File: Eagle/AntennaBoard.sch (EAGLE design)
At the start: 8 parts, among them IC1 MEGA8-P, IC2 MAX487*

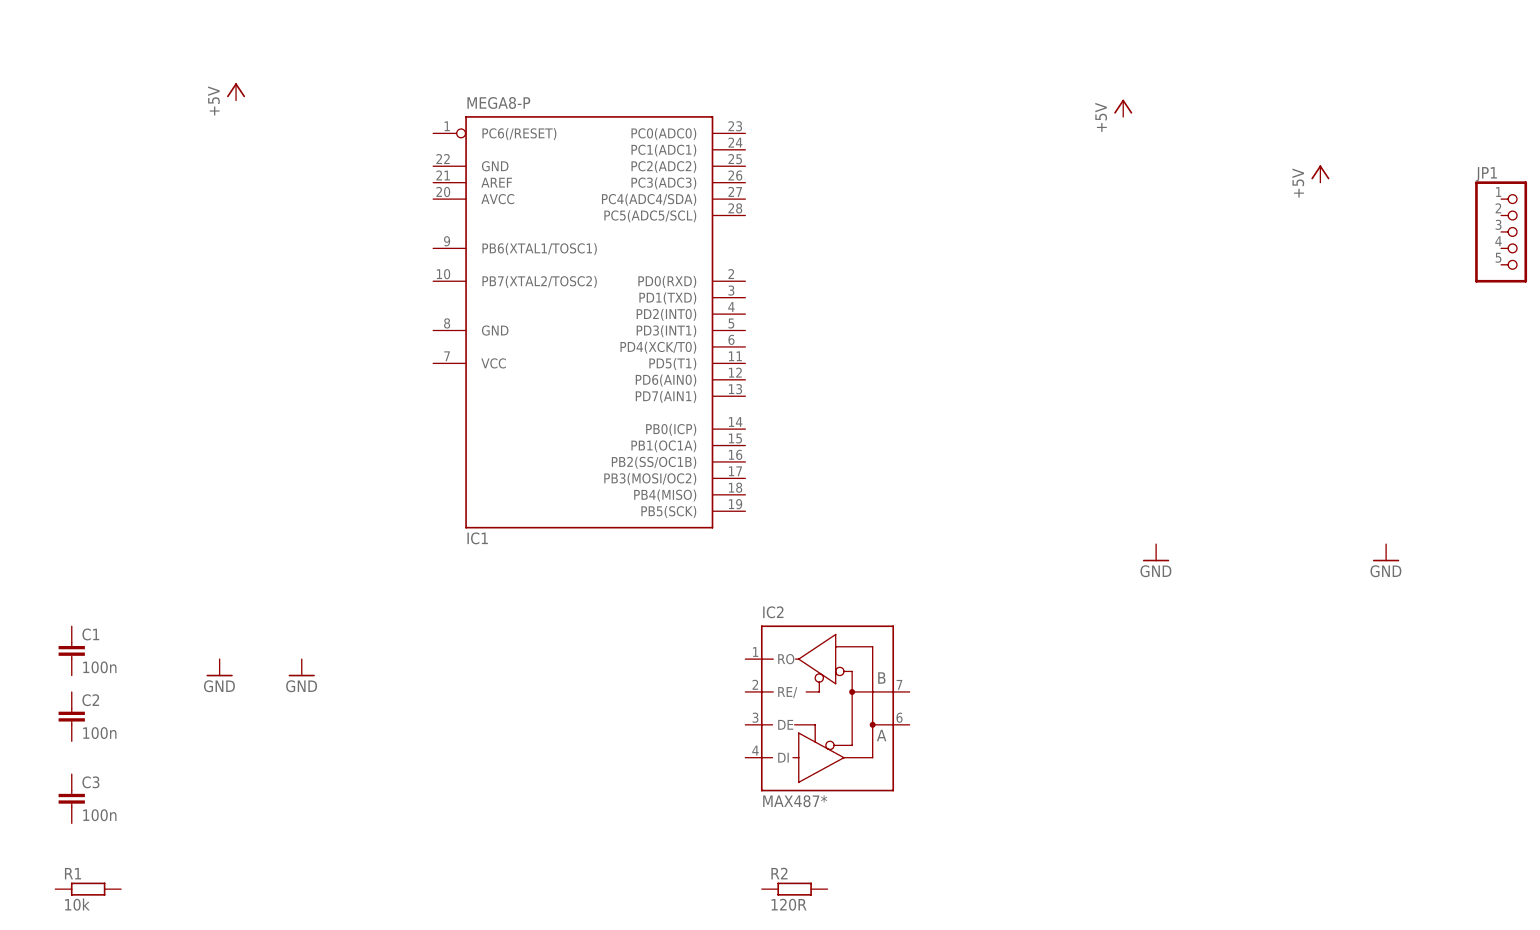
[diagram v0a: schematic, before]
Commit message: - AntennaBoard: finalized (?) and first board layout
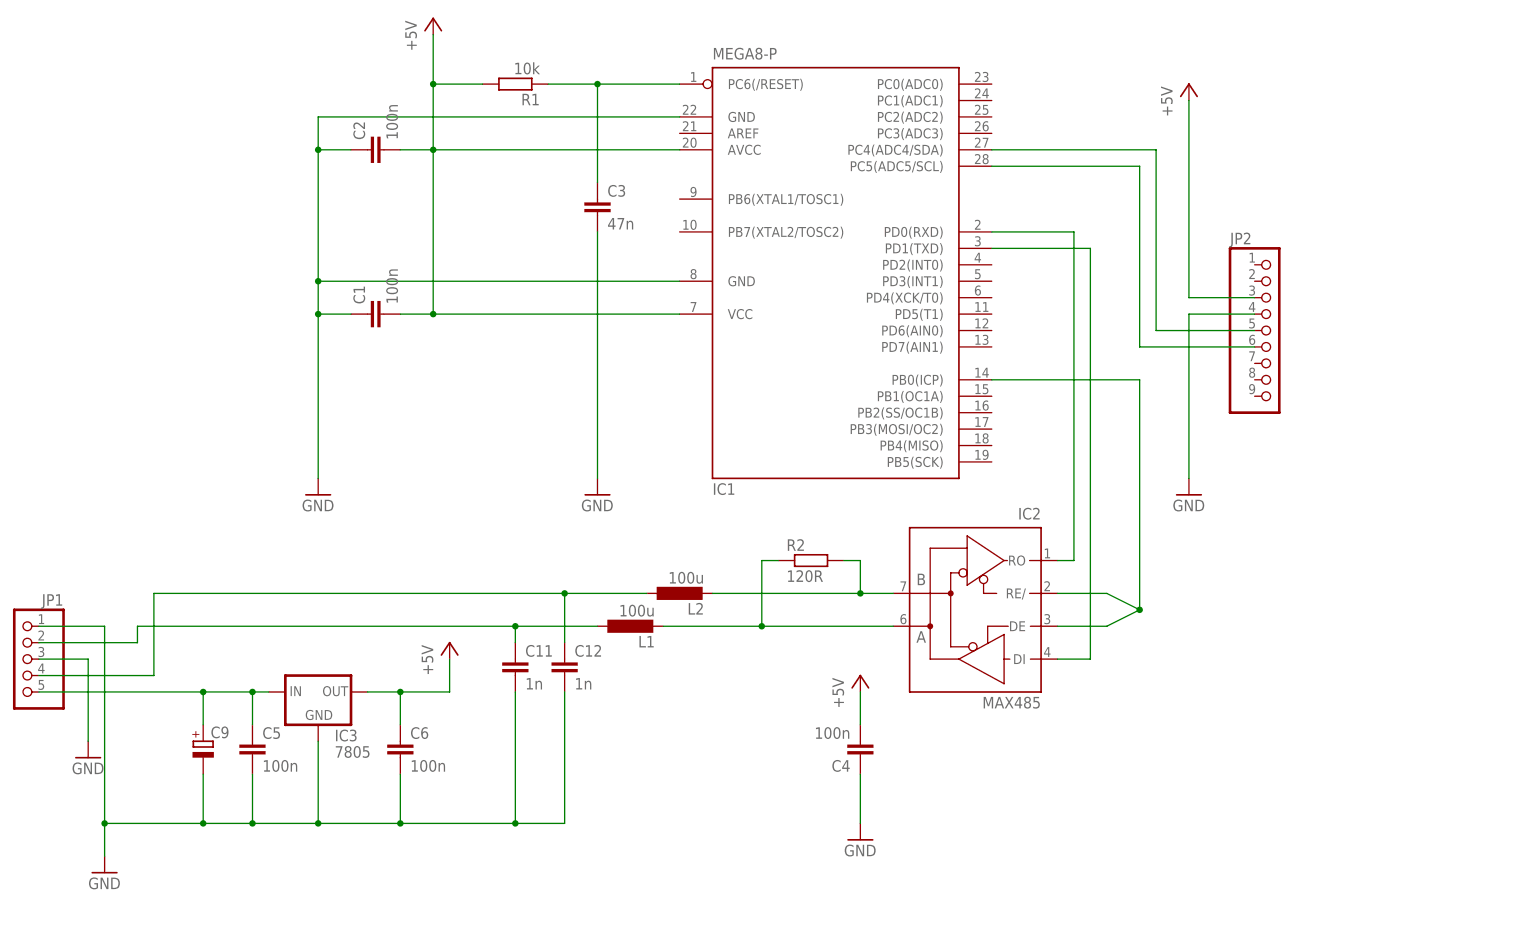
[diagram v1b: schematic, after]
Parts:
- added C11, C12: 1n, rcl:C-EU025-024X044
- added C4, C5, C6: 100n, rcl:C-EU050-024X044
- added C9: (no value), rcl:CPOL-EUE5-10.5
- added IC3: 7805, v-reg:78XXL
- added JP2: (no value), pinhead:PINHD-1X9
- added L1, L2: 100u, rcl:L-EU0207/12
- C3: value 100n -> 47n
- IC2: value MAX487* -> MAX485
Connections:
- new net +5V: C1.2, C2.2, C4.2, C6.1, IC1.AVCC, IC1.VCC@1, IC3.OUT, JP2.3, R1.2
- new net GND: C1.1, C11.2, C12.2, C2.1, C3.2, C4.1, C5.2, C6.2, C9.-, IC1.GND, IC1.GND@1, IC3.GND, JP1.1, JP1.3, JP2.4
- new net N$1: C5.1, C9.+, IC3.IN, JP1.5
- new net N$10: IC2G$1.B, L2.2, R2.2
- new net N$11: C11.1, JP1.2, L1.1
- new net N$2: IC2G$1.A, L1.2, R2.1
- new net N$3: C12.1, JP1.4, L2.1
- new net N$4: IC1.PC5(ADC5/SCL), JP2.6
- new net N$5: C3.1, IC1.PC6(/RESET), R1.1
- new net N$6: IC1.PC4(ADC4/SDA), JP2.5
- new net N$7: IC1.PB0(ICP), IC2G$1.DE, IC2G$1.RE/
- new net N$8: IC1.PD0(RXD), IC2G$1.RO
- new net N$9: IC1.PD1(TXD), IC2G$1.DI
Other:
- moved on the sheet: C1, C2, C3, IC1, IC2, JP1, R1, R2

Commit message: - IPS-Header added to AntennaBoard, U.Radig layout
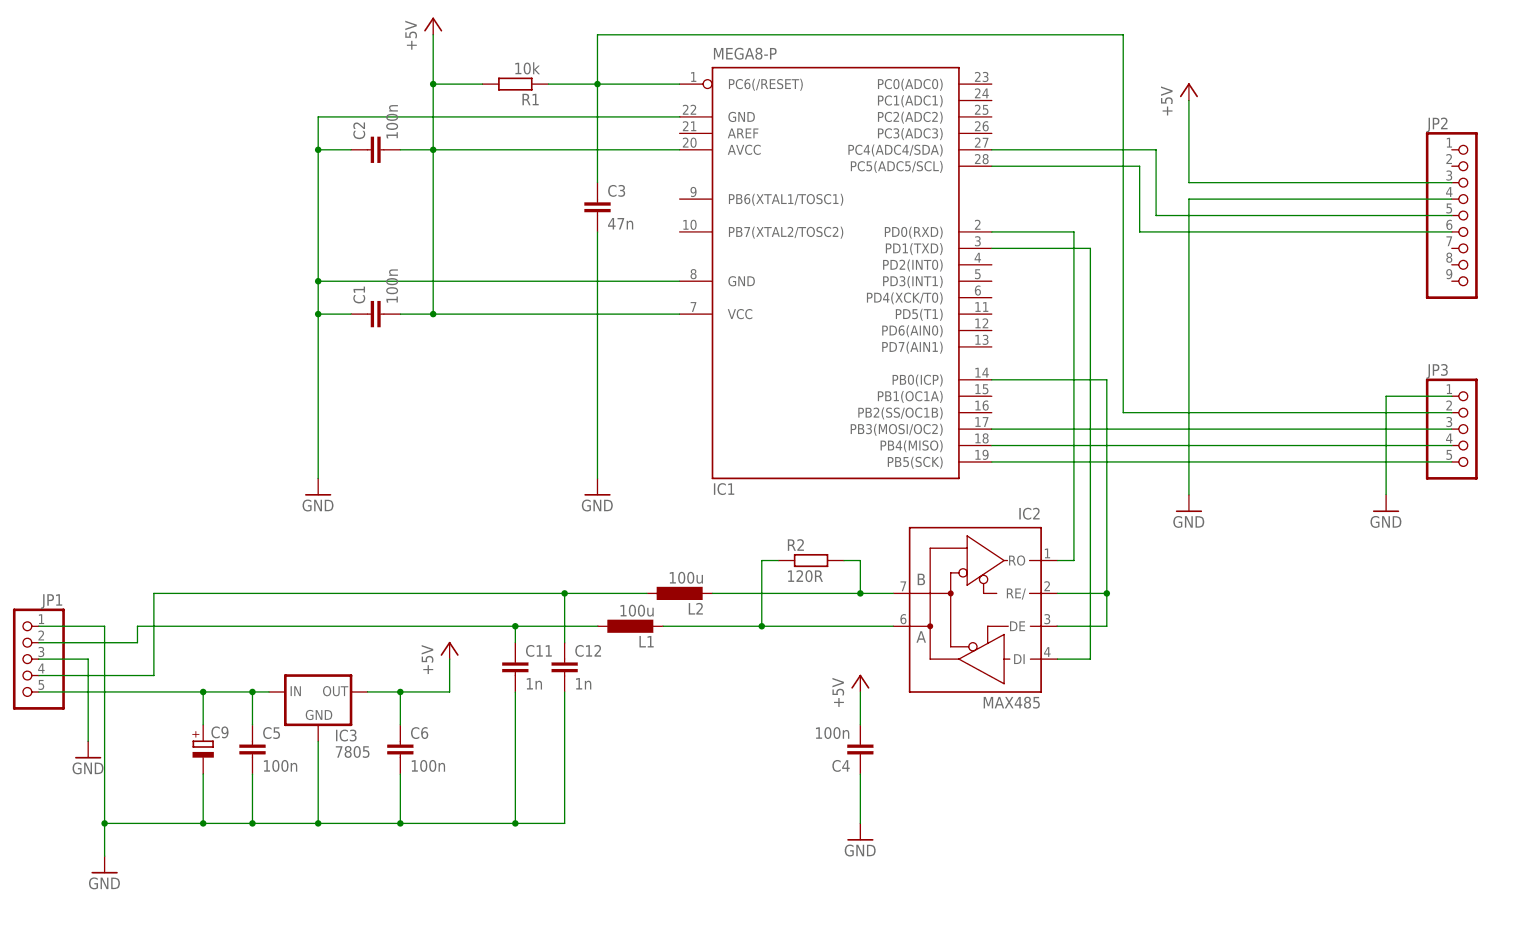
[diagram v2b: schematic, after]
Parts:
- added JP3: (no value), pinhead:PINHD-1X5
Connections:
- new net N$13: IC1.PB3(MOSI/OC2), JP3.3
- new net N$14: IC1.PB4(MISO), JP3.4
- new net N$15: IC1.PB5(SCK), JP3.5
- net GND: now also JP3.1
- net N$5: now also JP3.2
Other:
- moved on the sheet: JP2
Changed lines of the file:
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@@
 <part name="L2" library="rcl" deviceset="L-EU" device="0207/12" value="100u"/>
 <part name="GND3" library="supply1" deviceset="GND" device=""/>
+<part name="JP3" library="pinhead" deviceset="PINHD-1X5" device=""/>
+<part name="GND7" library="supply1" deviceset="GND" device=""/>
 </parts>
 <sheets>
@@
 <instance part="GND1" gate="1" x="58.42" y="104.14"/>
 <instance part="GND2" gate="1" x="25.4" y="45.72"/>
-<instance part="GND4" gate="1" x="193.04" y="104.14"/>
+<instance part="GND4" gate="1" x="193.04" y="101.6"/>
 <instance part="C4" gate="G$1" x="142.24" y="63.5" rot="R180"/>
-<instance part="JP2" gate="A" x="205.74" y="129.54"/>
+<instance part="JP2" gate="A" x="236.22" y="147.32"/>
 <instance part="IC3" gate="A" x="58.42" y="73.66"/>
 <instance part="C5" gate="G$1" x="48.26" y="66.04"/>
@@
 <instance part="L2" gate="G$1" x="114.3" y="88.9" rot="R90"/>
 <instance part="GND3" gate="1" x="101.6" y="104.14"/>
+<instance part="JP3" gate="A" x="236.22" y="114.3"/>
+<instance part="GND7" gate="1" x="223.52" y="101.6"/>
 </instances>
 <busses>
@@
 <segment>
 <pinref part="JP2" gate="A" pin="4"/>
-<wire x1="203.2" y1="132.08" x2="193.04" y2="132.08" width="0.1524" layer="91"/>
+<wire x1="233.68" y1="149.86" x2="193.04" y2="149.86" width="0.1524" layer="91"/>
 <pinref part="GND4" gate="1" pin="GND"/>
-<wire x1="193.04" y1="132.08" x2="193.04" y2="106.68" width="0.1524" layer="91"/>
+<wire x1="193.04" y1="149.86" x2="193.04" y2="104.14" width="0.1524" layer="91"/>
 </segment>
 <segment>
@@
 <pinref part="C3" gate="G$1" pin="2"/>
 <wire x1="101.6" y1="106.68" x2="101.6" y2="144.78" width="0.1524" layer="91"/>
+</segment>
+<segment>
+<pinref part="JP3" gate="A" pin="1"/>
+<wire x1="233.68" y1="119.38" x2="223.52" y2="119.38" width="0.1524" layer="91"/>
+<pinref part="GND7" gate="1" pin="GND"/>
+<wire x1="223.52" y1="119.38" x2="223.52" y2="104.14" width="0.1524" layer="91"/>
 </segment>
 </net>
@@
 <wire x1="101.6" y1="167.64" x2="101.6" y2="152.4" width="0.1524" layer="91"/>
 <junction x="101.6" y="167.64"/>
+<pinref part="JP3" gate="A" pin="2"/>
+<wire x1="233.68" y1="116.84" x2="182.88" y2="116.84" width="0.1524" layer="91"/>
+<wire x1="182.88" y1="116.84" x2="182.88" y2="175.26" width="0.1524" layer="91"/>
+<wire x1="182.88" y1="175.26" x2="101.6" y2="175.26" width="0.1524" layer="91"/>
+<wire x1="101.6" y1="175.26" x2="101.6" y2="167.64" width="0.1524" layer="91"/>
 </segment>
 </net>
@@
 <segment>
 <pinref part="JP2" gate="A" pin="3"/>
-<wire x1="203.2" y1="134.62" x2="193.04" y2="134.62" width="0.1524" layer="91"/>
+<wire x1="233.68" y1="152.4" x2="193.04" y2="152.4" width="0.1524" layer="91"/>
 <pinref part="P+3" gate="1" pin="+5V"/>
-<wire x1="193.04" y1="134.62" x2="193.04" y2="165.1" width="0.1524" layer="91"/>
+<wire x1="193.04" y1="152.4" x2="193.04" y2="165.1" width="0.1524" layer="91"/>
 </segment>
 </net>
@@
 <pinref part="IC1" gate="G$1" pin="PC5(ADC5/SCL)"/>
 <wire x1="162.56" y1="154.94" x2="185.42" y2="154.94" width="0.1524" layer="91"/>
-<wire x1="185.42" y1="154.94" x2="185.42" y2="127" width="0.1524" layer="91"/>
+<wire x1="185.42" y1="154.94" x2="185.42" y2="144.78" width="0.1524" layer="91"/>
 <pinref part="JP2" gate="A" pin="6"/>
-<wire x1="185.42" y1="127" x2="203.2" y2="127" width="0.1524" layer="91"/>
+<wire x1="185.42" y1="144.78" x2="233.68" y2="144.78" width="0.1524" layer="91"/>
 </segment>
 </net>
@@
 <pinref part="IC1" gate="G$1" pin="PC4(ADC4/SDA)"/>
 <wire x1="162.56" y1="157.48" x2="187.96" y2="157.48" width="0.1524" layer="91"/>
-<wire x1="187.96" y1="157.48" x2="187.96" y2="129.54" width="0.1524" layer="91"/>
+<wire x1="187.96" y1="157.48" x2="187.96" y2="147.32" width="0.1524" layer="91"/>
 <pinref part="JP2" gate="A" pin="5"/>
-<wire x1="187.96" y1="129.54" x2="203.2" y2="129.54" width="0.1524" layer="91"/>
+<wire x1="187.96" y1="147.32" x2="233.68" y2="147.32" width="0.1524" layer="91"/>
 </segment>
 </net>
 <net name="N$7" class="0">
 <segment>
+<wire x1="180.34" y1="88.9" x2="180.34" y2="121.92" width="0.1524" layer="91"/>
+<pinref part="IC1" gate="G$1" pin="PB0(ICP)"/>
+<wire x1="180.34" y1="121.92" x2="162.56" y2="121.92" width="0.1524" layer="91"/>
 <pinref part="IC2" gate="G$1" pin="RE/"/>
 <wire x1="172.72" y1="88.9" x2="180.34" y2="88.9" width="0.1524" layer="91"/>
-<wire x1="180.34" y1="88.9" x2="185.42" y2="86.36" width="0.1524" layer="91"/>
 <pinref part="IC2" gate="G$1" pin="DE"/>
-<wire x1="185.42" y1="86.36" x2="180.34" y2="83.82" width="0.1524" layer="91"/>
 <wire x1="180.34" y1="83.82" x2="172.72" y2="83.82" width="0.1524" layer="91"/>
-<junction x="185.42" y="86.36"/>
-<wire x1="185.42" y1="86.36" x2="185.42" y2="121.92" width="0.1524" layer="91"/>
-<pinref part="IC1" gate="G$1" pin="PB0(ICP)"/>
-<wire x1="185.42" y1="121.92" x2="162.56" y2="121.92" width="0.1524" layer="91"/>
+<wire x1="180.34" y1="88.9" x2="180.34" y2="83.82" width="0.1524" layer="91"/>
+<junction x="180.34" y="88.9"/>
 </segment>
 </net>
@@
 </segment>
 </net>
+<net name="N$13" class="0">
+<segment>
+<pinref part="IC1" gate="G$1" pin="PB3(MOSI/OC2)"/>
+<pinref part="JP3" gate="A" pin="3"/>
+<wire x1="162.56" y1="114.3" x2="233.68" y2="114.3" width="0.1524" layer="91"/>
+</segment>
+</net>
+<net name="N$14" class="0">
+<segment>
+<pinref part="JP3" gate="A" pin="4"/>
+<pinref part="IC1" gate="G$1" pin="PB4(MISO)"/>
+<wire x1="233.68" y1="111.76" x2="162.56" y2="111.76" width="0.1524" layer="91"/>
+</segment>
+</net>
+<net name="N$15" class="0">
+<segment>
+<pinref part="IC1" gate="G$1" pin="PB5(SCK)"/>
+<pinref part="JP3" gate="A" pin="5"/>
+<wire x1="162.56" y1="109.22" x2="233.68" y2="109.22" width="0.1524" layer="91"/>
+</segment>
+</net>

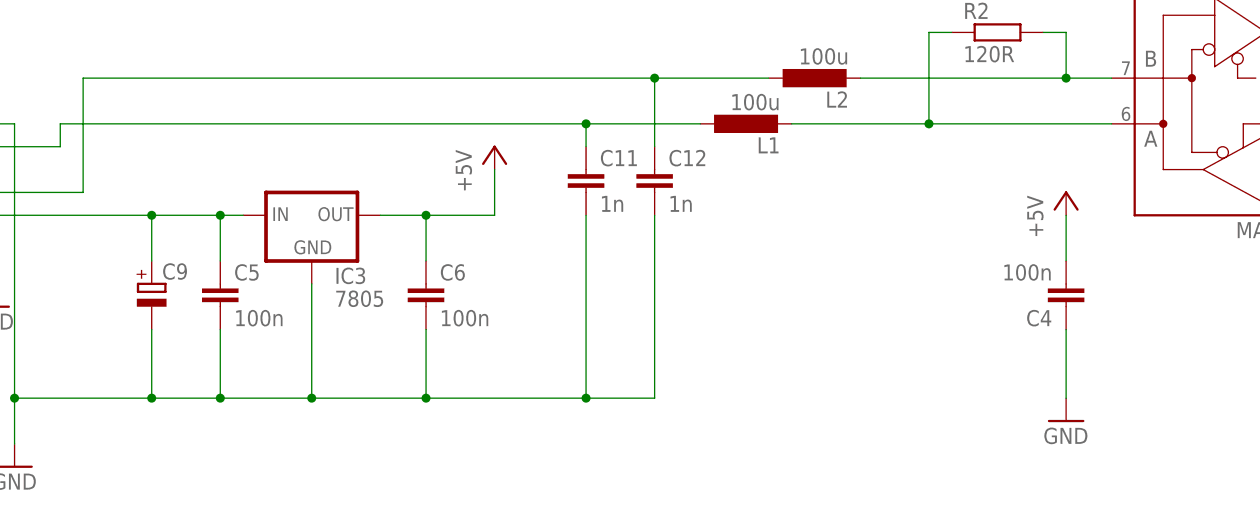
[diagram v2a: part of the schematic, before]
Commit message: - AntennaBoard: ERC errors fixed, worked on board and DRC - PowerSupply: ERC & DRC errors fixed
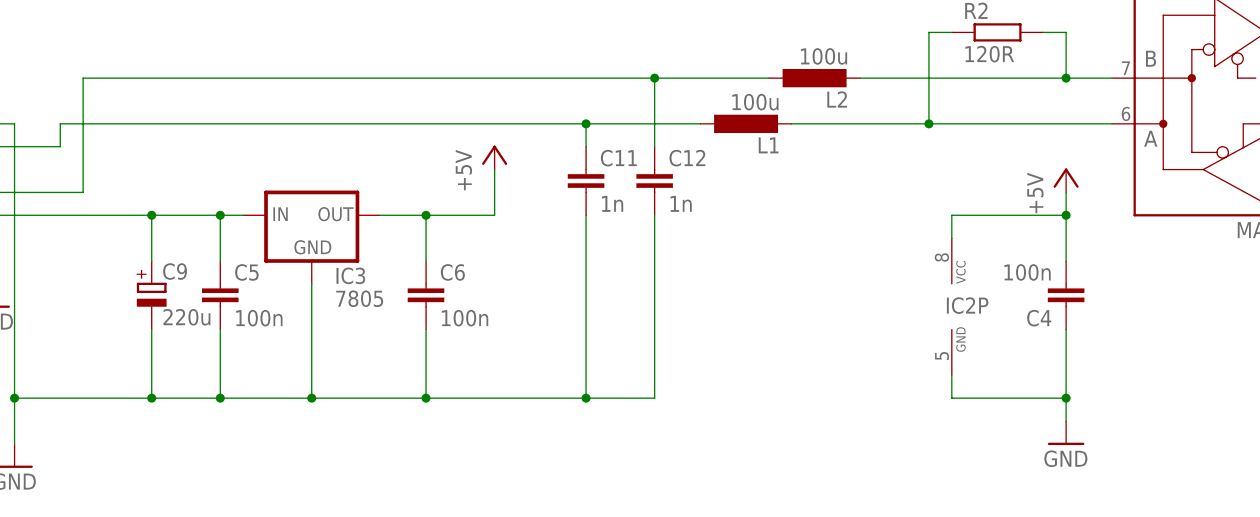
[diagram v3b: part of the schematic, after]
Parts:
- C9: value (none) -> 220u
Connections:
- net +5V: now also IC2P.VCC
- net GND: now also IC2P.GND
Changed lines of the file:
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@@
 <layer number="91" name="Nets" color="2" fill="1" visible="yes" active="yes"/>
 <layer number="92" name="Busses" color="1" fill="1" visible="yes" active="yes"/>
-<layer number="93" name="Pins" color="2" fill="1" visible="no" active="yes"/>
+<layer number="93" name="Pins" color="2" fill="1" visible="yes" active="yes"/>
 <layer number="94" name="Symbols" color="4" fill="1" visible="yes" active="yes"/>
 <layer number="95" name="Names" color="7" fill="1" visible="yes" active="yes"/>
@@
 <part name="C5" library="rcl" deviceset="C-EU" device="050-024X044" value="100n"/>
 <part name="C6" library="rcl" deviceset="C-EU" device="050-024X044" value="100n"/>
-<part name="C9" library="rcl" deviceset="CPOL-EU" device="E5-10.5"/>
+<part name="C9" library="rcl" deviceset="CPOL-EU" device="E5-10.5" value="220u"/>
 <part name="P+4" library="supply1" deviceset="+5V" device=""/>
 <part name="GND5" library="supply1" deviceset="GND" device=""/>
@@
 <instance part="P+4" gate="1" x="78.74" y="81.28"/>
 <instance part="GND5" gate="1" x="22.86" y="63.5"/>
-<instance part="P+6" gate="1" x="142.24" y="76.2"/>
-<instance part="GND6" gate="1" x="142.24" y="50.8"/>
+<instance part="P+6" gate="1" x="142.24" y="78.74"/>
+<instance part="GND6" gate="1" x="142.24" y="48.26"/>
 <instance part="C11" gate="G$1" x="88.9" y="78.74"/>
 <instance part="C12" gate="G$1" x="96.52" y="78.74"/>
@@
 <instance part="JP3" gate="A" x="236.22" y="114.3"/>
 <instance part="GND7" gate="1" x="223.52" y="101.6"/>
+<instance part="IC2" gate="P" x="129.54" y="63.5"/>
 </instances>
 <busses>
@@
 <pinref part="GND6" gate="1" pin="GND"/>
 <wire x1="142.24" y1="60.96" x2="142.24" y2="53.34" width="0.1524" layer="91"/>
+<pinref part="IC2" gate="P" pin="GND"/>
+<wire x1="142.24" y1="53.34" x2="142.24" y2="50.8" width="0.1524" layer="91"/>
+<wire x1="129.54" y1="55.88" x2="129.54" y2="53.34" width="0.1524" layer="91"/>
+<wire x1="129.54" y1="53.34" x2="142.24" y2="53.34" width="0.1524" layer="91"/>
+<junction x="142.24" y="53.34"/>
 </segment>
 <segment>
@@
 <pinref part="P+6" gate="1" pin="+5V"/>
 <pinref part="C4" gate="G$1" pin="2"/>
+<wire x1="142.24" y1="76.2" x2="142.24" y2="73.66" width="0.1524" layer="91"/>
 <wire x1="142.24" y1="73.66" x2="142.24" y2="68.58" width="0.1524" layer="91"/>
+<wire x1="142.24" y1="73.66" x2="129.54" y2="73.66" width="0.1524" layer="91"/>
+<junction x="142.24" y="73.66"/>
+<pinref part="IC2" gate="P" pin="VCC"/>
+<wire x1="129.54" y1="73.66" x2="129.54" y2="71.12" width="0.1524" layer="91"/>
 </segment>
 <segment>
@@
 </sheet>
 </sheets>
+<errors>
+</errors>
 </schematic>
 </drawing>
